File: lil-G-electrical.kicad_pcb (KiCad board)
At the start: 2 copper layers, 65 x 56 mm, 7 parts, among them J1 GPIO, U2 TPS565208

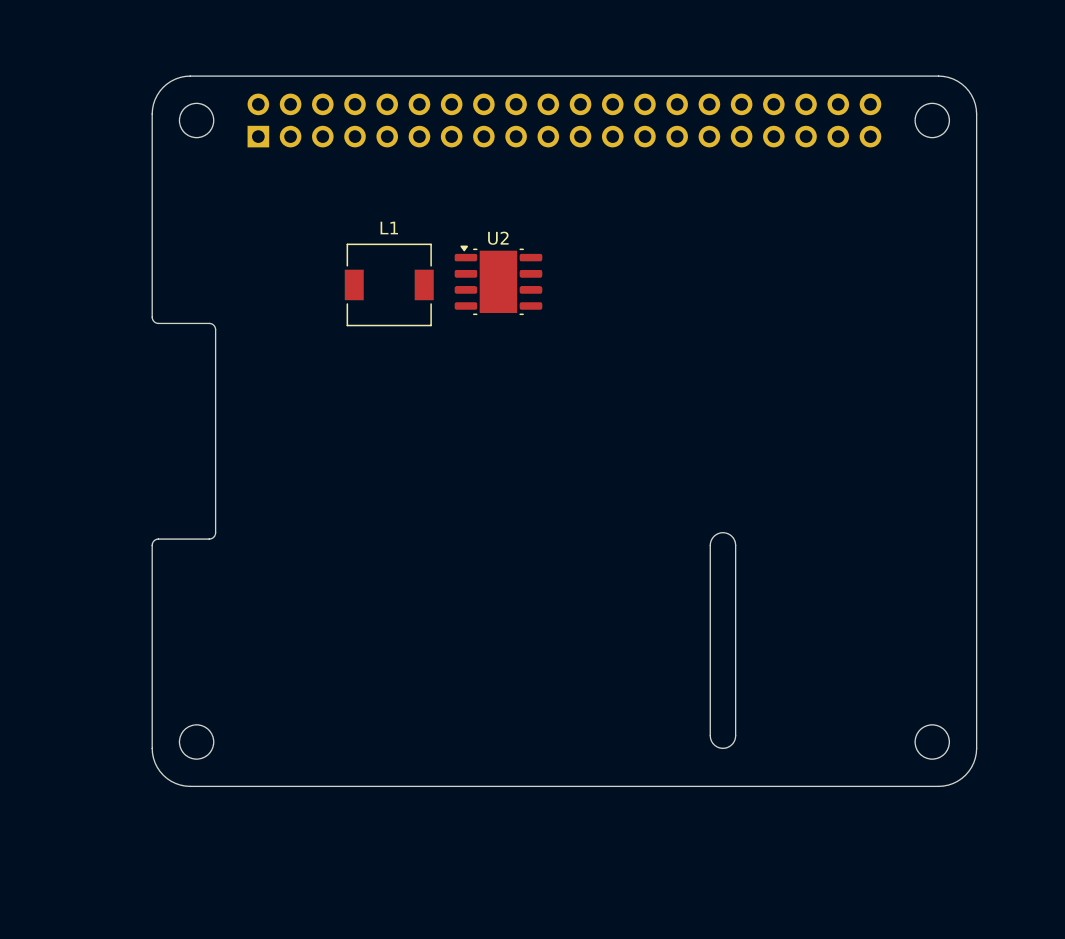
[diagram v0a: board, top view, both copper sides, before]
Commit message: finished layout of dc drivers and power regulation
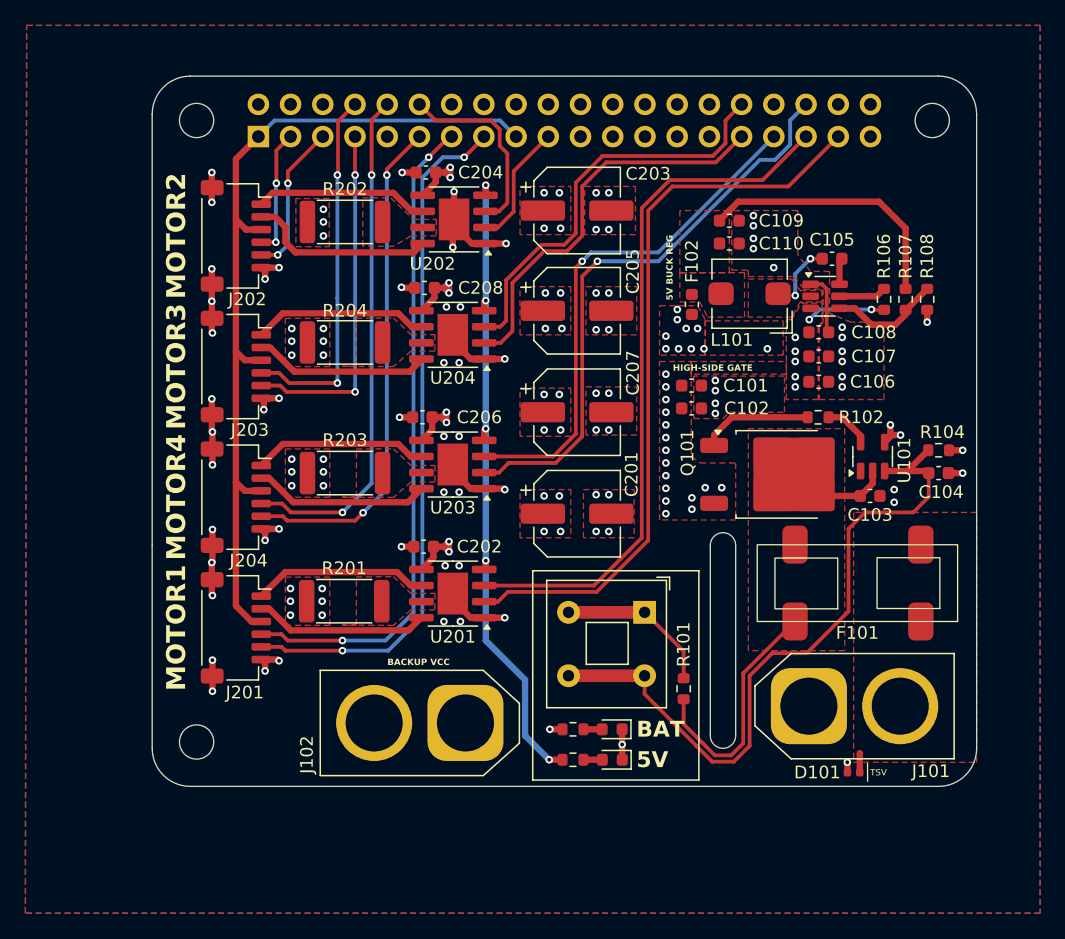
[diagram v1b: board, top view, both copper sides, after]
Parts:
- removed MH4: MountingHole_2.7mm_M2.5, MountingHole:MountingHole_2.7mm_M2.5
- added C101: 22uF, Capacitor_SMD:C_0603_1608Metric, F.Cu at (142.5, 68.4)
- added C102: 22uF, Capacitor_SMD:C_0603_1608Metric, F.Cu at (142.5, 70.2)
- added C103: 10uF, Capacitor_SMD:C_0603_1608Metric, F.Cu at (156.6, 77.1)
- added C104: 0.1uF, Capacitor_SMD:C_0603_1608Metric, F.Cu at (162.0, 75.3)
- added C105: 0.1uF, Capacitor_SMD:C_0603_1608Metric, F.Cu at (153.6, 58.4)
- added C106: 10uF, Capacitor_SMD:C_0603_1608Metric, F.Cu at (152.6, 68.1)
- added C107: 10uF, Capacitor_SMD:C_0603_1608Metric, F.Cu at (152.6, 66.1)
- added C108: 0.1uF, Capacitor_SMD:C_0603_1608Metric, F.Cu at (152.6, 64.2)
- added C109: 22uF, Capacitor_SMD:C_0603_1608Metric, F.Cu at (145.5, 55.4)
- added C110: 22uF, Capacitor_SMD:C_0603_1608Metric, F.Cu at (145.5, 57.2)
- added C201: 100uF, Capacitor_SMD:CP_Elec_6.3x7.7, F.Cu at (133.5, 78.5)
- added C202: 0.22uF, Capacitor_SMD:C_0603_1608Metric, F.Cu at (121.4, 81.1)
- added C203: 100uF, Capacitor_SMD:CP_Elec_6.3x7.7, F.Cu at (133.5, 54.6)
- added C204: 0.22uF, Capacitor_SMD:C_0603_1608Metric, F.Cu at (121.6, 51.6)
- added C205: 100uF, Capacitor_SMD:CP_Elec_6.3x7.7, F.Cu at (133.5, 62.5)
- added C206: 0.22uF, Capacitor_SMD:C_0603_1608Metric, F.Cu at (121.3, 70.9)
- added C207: 100uF, Capacitor_SMD:CP_Elec_6.3x7.7, F.Cu at (133.5, 70.5)
- added C208: 0.22uF, Capacitor_SMD:C_0603_1608Metric, F.Cu at (121.5, 60.7)
- added D101: GG0402126R042P, Diode_SMD:D_0402_1005Metric, F.Cu at (155.3, 98.9)
- added D102: GREEN, LED_SMD:LED_0603_1608Metric, F.Cu at (136.3, 95.5)
- added D103: GREEN, LED_SMD:LED_0603_1608Metric, F.Cu at (136.3, 97.9)
- added F101: 10A, lilG_footprints:LittleFuse_Mini_100_SMD, F.Cu at (155.6, 84.0)
- added F102: 5A, Fuse:Fuse_0603_1608Metric, F.Cu at (142.6, 62.0)
- added J101: XT-60, Connector_AMASS:AMASS_XT60-M_1x02_P7.20mm_Vertical, F.Cu at (151.8, 93.7)
- added J102: XT-60, Connector_AMASS:AMASS_XT60-M_1x02_P7.20mm_Vertical, F.Cu at (124.7, 95.0)
- added J201: JST-SH, Connector_JST:JST_SH_SM06B-SRSS-TB_1x06-1MP_P1.00mm_Horizontal, F.Cu at (106.6, 87.5)
- added J202: JST-SH, Connector_JST:JST_SH_SM06B-SRSS-TB_1x06-1MP_P1.00mm_Horizontal, F.Cu at (106.6, 56.6)
- added J203: JST-SH, Connector_JST:JST_SH_SM06B-SRSS-TB_1x06-1MP_P1.00mm_Horizontal, F.Cu at (106.6, 66.9)
- added J204: JST-SH, Connector_JST:JST_SH_SM06B-SRSS-TB_1x06-1MP_P1.00mm_Horizontal, F.Cu at (106.6, 77.2)
- added Q101: STD26P3LLH6, Package_TO_SOT_SMD:TO-252-2, F.Cu at (149.3, 75.4)
- added R101: 10k, Resistor_SMD:R_0603_1608Metric, F.Cu at (141.9, 92.3)
- added R102: 22, Resistor_SMD:R_0603_1608Metric, F.Cu at (152.5, 70.9)
- added R103: 10k, Resistor_SMD:R_0603_1608Metric, F.Cu at (133.2, 95.5)
- added R104: 10k, Resistor_SMD:R_0603_1608Metric, F.Cu at (162.0, 73.5)
- added R105: 1k, Resistor_SMD:R_0603_1608Metric, F.Cu at (133.2, 97.9)
- added R106: 10k, Resistor_SMD:R_0603_1608Metric, F.Cu at (157.7, 61.6)
- added R107: 54.9k, Resistor_SMD:R_0603_1608Metric, F.Cu at (159.4, 61.6)
- added R108: 10k, Resistor_SMD:R_0603_1608Metric, F.Cu at (161.1, 61.6)
- added R201: 500m, Resistor_SMD:R_2512_6332Metric, F.Cu at (115.1, 85.4)
- added R202: 500m, Resistor_SMD:R_2512_6332Metric, F.Cu at (115.2, 55.5)
- added R203: 500m, Resistor_SMD:R_2512_6332Metric, F.Cu at (115.2, 75.3)
- added R204: 500m, Resistor_SMD:R_2512_6332Metric, F.Cu at (115.2, 65.0)
- added SW101: PVA1EE, Button_Switch_THT:SW_Push_2P1T_Toggle_CK_PVA1xxH4xxxxxxV2, F.Cu at (138.8, 86.3)
- added U101: MCP1415, Package_TO_SOT_SMD:SOT-23-5, F.Cu at (156.8, 74.0)
- added U201: A4950E, Package_SO:SOIC-8-1EP_3.9x4.9mm_P1.27mm_EP2.41x3.3mm, F.Cu at (123.7, 84.8)
- added U202: A4950E, Package_SO:SOIC-8-1EP_3.9x4.9mm_P1.27mm_EP2.41x3.3mm, F.Cu at (123.8, 55.3)
- added U203: A4950E, Package_SO:SOIC-8-1EP_3.9x4.9mm_P1.27mm_EP2.41x3.3mm, F.Cu at (123.7, 74.6)
- added U204: A4950E, Package_SO:SOIC-8-1EP_3.9x4.9mm_P1.27mm_EP2.41x3.3mm, F.Cu at (123.7, 64.4)
- L101: renamed from L1; value L_Small -> 3.3uH; footprint Inductor_SMD:L_6.3x6.3_H3 -> Inductor_SMD:L_Bourns_SRP5030T
- U102: renamed from U2; footprint Package_SO:Texas_R-PDSO-G8_EP2.95x4.9mm_Mask2.4x3.1mm -> Package_TO_SOT_SMD:SOT-23-6
- moved L101 28.4 mm to (147.1, 61.2), turned to 180 degrees
- moved U102 25.8 mm to (153.1, 61.4)
- renumbered J1 to J103
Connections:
- J103 pad 10: /GPIO15/RXD0 -> /M4_ENC_A
- J103 pad 11: /GPIO17 -> /M4_ENC_B
- J103 pad 12: /GPIO18/PCM.CLK -> /M2_PWM
- J103 pad 13: /GPIO27 -> /M1_ENC_A
- J103 pad 15: /GPIO22 -> /M1_ENC_B
- J103 pad 16: /GPIO23 -> unconnected-(J103-Pin_16-Pad16)
- J103 pad 18: /GPIO24 -> unconnected-(J103-Pin_18-Pad18)
- J103 pad 19: /GPIO10/SPI0.MOSI -> /M2_DIR
- J103 pad 21: /GPIO9/SPI0.MISO -> unconnected-(J103-Pin_21-Pad21)
- J103 pad 22: /GPIO25 -> unconnected-(J103-Pin_22-Pad22)
- J103 pad 23: /GPIO11/SPI0.SCLK -> unconnected-(J103-Pin_23-Pad23)
- J103 pad 24: /GPIO8/SPI0.CE0 -> unconnected-(J103-Pin_24-Pad24)
- J103 pad 26: /GPIO7/SPI0.CE1 -> unconnected-(J103-Pin_26-Pad26)
- J103 pad 27: /ID_SDA -> unconnected-(J103-Pin_27-Pad27)
- J103 pad 28: /ID_SCL -> unconnected-(J103-Pin_28-Pad28)
- J103 pad 29: /GPIO5 -> unconnected-(J103-Pin_29-Pad29)
- J103 pad 3: /GPIO2/SDA1 -> /M2_ENC_A
- J103 pad 31: /GPIO6 -> /M3_DIR
- J103 pad 32: /GPIO12/PWM0 -> /M3_PWM
- J103 pad 33: /GPIO13/PWM1 -> /M4_PWM
- J103 pad 35: /GPIO19/PCM.FS -> /M1_PWM
- J103 pad 36: /GPIO16 -> /M4_DIR
- J103 pad 37: /GPIO26 -> /M1_DIR
- J103 pad 38: /GPIO20/PCM.DIN -> unconnected-(J103-Pin_38-Pad38)
- J103 pad 40: /GPIO21/PCM.DOUT -> unconnected-(J103-Pin_40-Pad40)
- J103 pad 5: /GPIO3/SCL1 -> /M2_ENC_B
- J103 pad 7: /GPIO4/GPCLK0 -> /M3_ENC_B
- J103 pad 8: /GPIO14/TXD0 -> /M3_ENC_A
- L101 pad 1: unconnected-(L1-Pad1) -> Net-(U102-SW)
- L101 pad 2: unconnected-(L1-Pad2) -> Net-(C109-Pad1)
- U102 pad 1: unconnected-(U2-GND-Pad1) -> GND
- U102 pad 2: unconnected-(U2-SW-Pad2) -> Net-(U102-SW)
- U102 pad 3: unconnected-(U2-VIN-Pad3) -> VCC
- U102 pad 4: unconnected-(U2-VFB-Pad4) -> Net-(U102-VFB)
- U102 pad 5: unconnected-(U2-EN-Pad5) -> Net-(U102-EN)
- U102 pad 6: unconnected-(U2-VBST-Pad6) -> Net-(U102-VBST)
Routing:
- net +5V: track 0.00 -> 79.1 mm, vias 0 -> 15
- net +3V3: track 0.00 -> 68.5 mm
- net GND: track 0.00 -> 67.8 mm, vias 0 -> 104
- net /M1_DIR: track 0.00 -> 58.3 mm
- net /PWR_EN: track 0.00 -> 55.5 mm
- net /M1_PWM: track 0.00 -> 55.3 mm
- net /M1_ENC_B: track 0.00 -> 54.8 mm, vias 0 -> 2
- net /M1_ENC_A: track 0.00 -> 52.0 mm, vias 0 -> 2
- net /M4_DIR: track 0.00 -> 45.9 mm, vias 0 -> 1
- net /M4_PWM: track 0.00 -> 41.0 mm, vias 0 -> 1
- net /M4_ENC_A: track 0.00 -> 40.3 mm, vias 0 -> 2
- net /M4_ENC_B: track 0.00 -> 39.9 mm, vias 0 -> 2
- net /M3_PWM: track 0.00 -> 32.8 mm
- net /M3_DIR: track 0.00 -> 31.5 mm
- net /M3_ENC_A: track 0.00 -> 28.9 mm, vias 0 -> 2
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- added copper zone on F.Cu, net +5V
- added copper zone on In2.Cu, net +5V
- added copper zone on B.Cu, net GND
- added copper zone on F.Cu, net GND
- added copper zone on In1.Cu, net GND
- added copper zone on F.Cu, net Net-(C109-Pad1)
- added copper zone on F.Cu, net Net-(D101-K)
- added copper zone on F.Cu, net Net-(Q101-D)
- added copper zone on F.Cu, net Net-(U102-SW)
- added copper zone on F.Cu, net Net-(U201-LSS)
- added copper zone on F.Cu, net Net-(U202-LSS)
- added copper zone on F.Cu, net Net-(U203-LSS)
- added copper zone on F.Cu, net Net-(U204-LSS)
- added copper zone on F.Cu, net VCC
- added copper zone on In2.Cu, net VCC
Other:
- outline, holes or cut-outs redrawn
- copper layers 2 -> 4
- board text added: "5V"
- board text added: "5V BUCK REG"
- board text added: "BACKUP VCC"
- board text added: "BAT"
- board text added: "HIGH-SIDE GATE"
- board text added: "MOTOR1"
- board text added: "MOTOR2"
- board text added: "MOTOR3"
- board text added: "MOTOR4"
- board text added: "TSV"

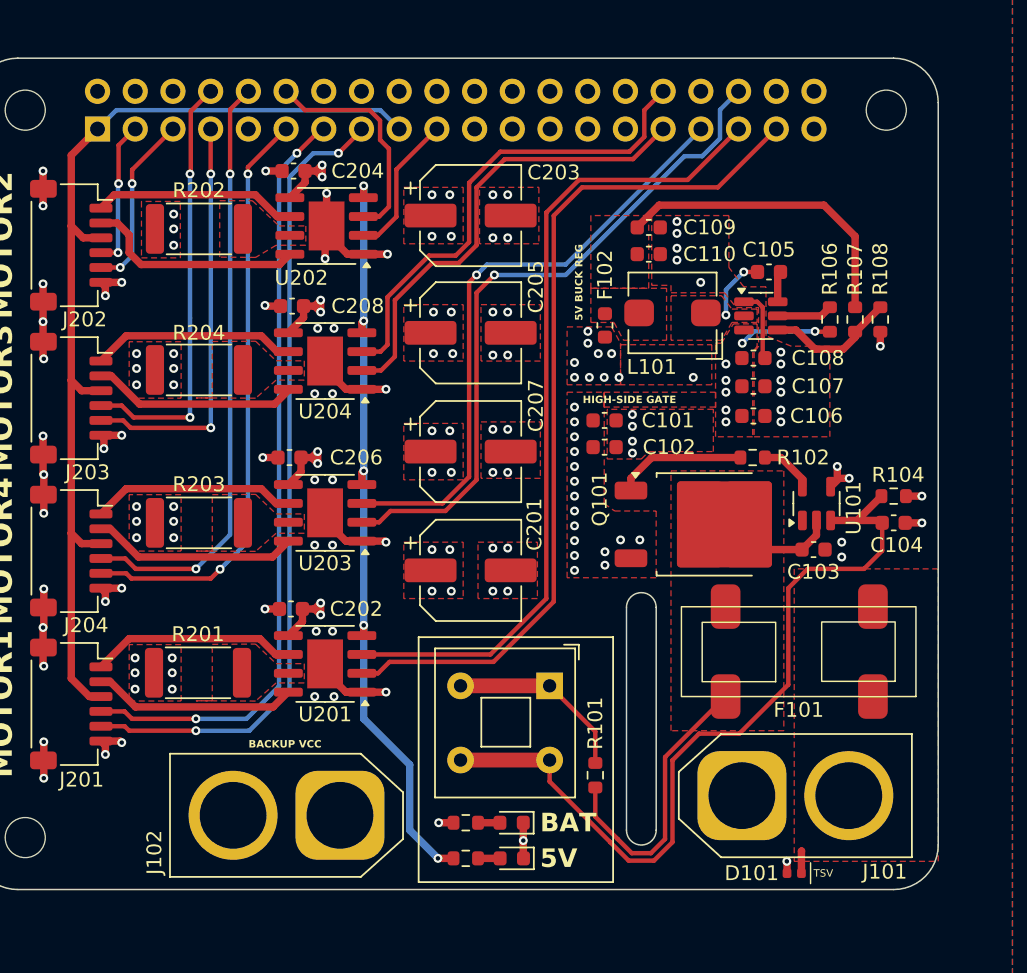
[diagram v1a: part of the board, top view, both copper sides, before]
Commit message: changed dimension of current sense resistor
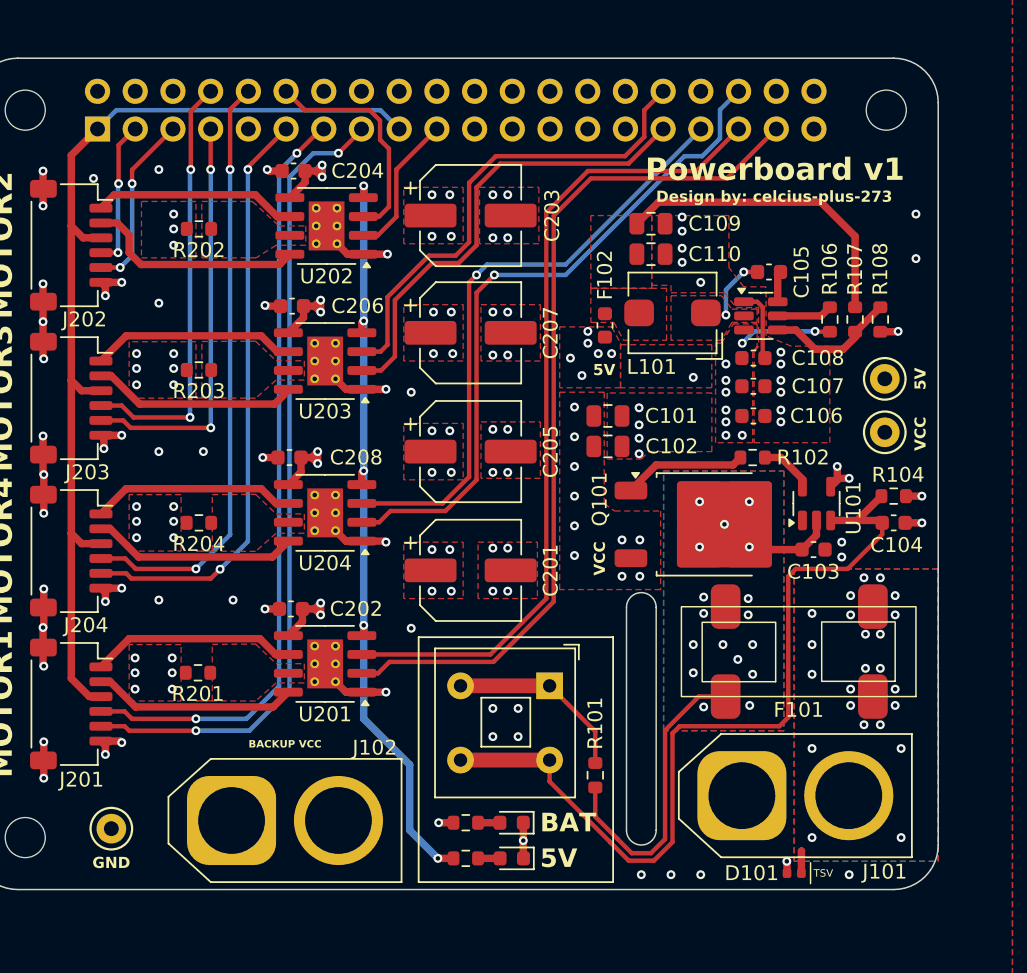
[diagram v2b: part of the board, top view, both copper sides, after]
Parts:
- added TP101: TestPoint, TestPoint:TestPoint_Keystone_5000-5004_Miniature, F.Cu at (161.4, 69.2)
- added TP102: TestPoint, TestPoint:TestPoint_Keystone_5000-5004_Miniature, F.Cu at (109.3, 95.9)
- added TP103: TestPoint, TestPoint:TestPoint_Keystone_5000-5004_Miniature, F.Cu at (161.4, 65.6)
- C101, C102, C109, C110: footprint Capacitor_SMD:C_0603_1608Metric -> Capacitor_SMD:C_0805_2012Metric
- F101: value 10A -> 01000065Z
- F102: value 5A -> 0686F5000
- R201, R202: footprint Resistor_SMD:R_2512_6332Metric -> Resistor_SMD:R_0603_1608Metric
- R203: renamed from R204; footprint Resistor_SMD:R_2512_6332Metric -> Resistor_SMD:R_0603_1608Metric
- R204: renamed from R203; footprint Resistor_SMD:R_2512_6332Metric -> Resistor_SMD:R_0603_1608Metric
- U201, U202: footprint Package_SO:SOIC-8-1EP_3.9x4.9mm_P1.27mm_EP2.41x3.3mm -> Package_SO:SOIC-8-1EP_3.9x4.9mm_P1.27mm_EP2.41x3.3mm_ThermalVias
- U203: renamed from U204; footprint Package_SO:SOIC-8-1EP_3.9x4.9mm_P1.27mm_EP2.41x3.3mm -> Package_SO:SOIC-8-1EP_3.9x4.9mm_P1.27mm_EP2.41x3.3mm_ThermalVias
- U204: renamed from U203; footprint Package_SO:SOIC-8-1EP_3.9x4.9mm_P1.27mm_EP2.41x3.3mm -> Package_SO:SOIC-8-1EP_3.9x4.9mm_P1.27mm_EP2.41x3.3mm_ThermalVias
- moved J102 7.31 mm to (117.4, 95.3), turned to 0 degrees
- moved C101 0.38 mm to (142.8, 68.1)
- moved C109 0.29 mm to (145.7, 55.1)
- moved C102 0.23 mm to (142.8, 70.2)
- moved C110 0.15 mm to (145.7, 57.2)
- renumbered C207 to C205, C208 to C206, C205 to C207, C206 to C208
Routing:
- net VCC: track 26.8 -> 59.9 mm, vias 48 -> 44
- net +5V: track 79.1 -> 109.9 mm, vias 15 -> 12
- net GND: track 67.8 -> 63.5 mm, vias 104 -> 109
- net /PWR_EN: track 55.5 -> 57.7 mm
- net Net-(Q101-D): track 25.4 -> 26.4 mm, vias 0 -> 17
- net Net-(D101-K): vias 0 -> 23
- added copper zone on B.Cu, net Net-(D101-K)
- added copper zone on B.Cu, net Net-(Q101-D)
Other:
- board text added: "Design by: celcius-plus-273"
- board text added: "GND"
- board text added: "Powerboard v1"
- board text added: "VCC"
- board text removed: "5V BUCK REG"
- board text removed: "HIGH-SIDE GATE"

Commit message: version 2 done
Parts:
- removed C101, C102, C109, C110: 22uF, Capacitor_SMD:C_0805_2012Metric
- removed C103, C106, C107: 10uF, Capacitor_SMD:C_0603_1608Metric
- removed C104, C105, C108: 0.1uF, Capacitor_SMD:C_0603_1608Metric
- removed C201, C203, C205, C207: 100uF, Capacitor_SMD:CP_Elec_6.3x7.7
- removed C202, C204, C206, C208: 0.22uF, Capacitor_SMD:C_0603_1608Metric
- removed D101: GG0402126R042P, Diode_SMD:D_0402_1005Metric
- removed D102, D103: GREEN, LED_SMD:LED_0603_1608Metric
- removed F101: 01000065Z, lilG_footprints:LittleFuse_Mini_100_SMD
- removed F102: 0686F5000, Fuse:Fuse_0603_1608Metric
- removed J101, J102: XT-60, Connector_AMASS:AMASS_XT60-M_1x02_P7.20mm_Vertical
- removed J103: GPIO, Connector_PinSocket_2.54mm:PinSocket_2x20_P2.54mm_Vertical
- removed J201, J202, J203, J204: JST-SH, Connector_JST:JST_SH_SM06B-SRSS-TB_1x06-1MP_P1.00mm_Horizontal
- removed L101: 3.3uH, Inductor_SMD:L_Bourns_SRP5030T
- removed Q101: STD26P3LLH6, Package_TO_SOT_SMD:TO-252-2
- removed R101, R103, R104, R106, R108: 10k, Resistor_SMD:R_0603_1608Metric
- removed R102: 22, Resistor_SMD:R_0603_1608Metric
- removed R105: 1k, Resistor_SMD:R_0603_1608Metric
- removed R107: 54.9k, Resistor_SMD:R_0603_1608Metric
- removed R201, R202, R203, R204: 500m, Resistor_SMD:R_0603_1608Metric
- removed SW101: PVA1EE, Button_Switch_THT:SW_Push_2P1T_Toggle_CK_PVA1xxH4xxxxxxV2
- removed TP101, TP102, TP103: TestPoint, TestPoint:TestPoint_Keystone_5000-5004_Miniature
- removed U101: MCP1415, Package_TO_SOT_SMD:SOT-23-5
- removed U102: TPS565208, Package_TO_SOT_SMD:SOT-23-6
- removed U201, U202, U203, U204: A4950E, Package_SO:SOIC-8-1EP_3.9x4.9mm_P1.27mm_EP2.41x3.3mm_ThermalVias
- added C1: 22uF, Capacitor_SMD:C_0805_2012Metric, F.Cu at (101.8, 97.2)
- added C10: 22uF, Capacitor_SMD:C_0805_2012Metric, F.Cu at (107.2, 90.3)
- added C11: 10uF, Capacitor_SMD:C_0603_1608Metric, F.Cu at (76.8, 95.5)
- added C12: 10uF, Capacitor_SMD:C_0603_1608Metric, F.Cu at (74.1, 96.2)
- added C13: 100n, Capacitor_SMD:C_0402_1005Metric, F.Cu at (77.2, 76.2)
- added C15: 100n, Capacitor_SMD:C_0402_1005Metric, F.Cu at (81.8, 81.0)
- added C16: 100n, Capacitor_SMD:C_0402_1005Metric, F.Cu at (85.6, 83.8)
- added C17: 100n, Capacitor_SMD:C_0402_1005Metric, F.Cu at (90.2, 71.9)
- added C18: 100n, Capacitor_SMD:C_0402_1005Metric, F.Cu at (91.5, 84.2)
- added C19: 100n, Capacitor_SMD:C_0402_1005Metric, F.Cu at (94.9, 73.9)
- added C2: 22uF, Capacitor_SMD:C_0805_2012Metric, F.Cu at (99.3, 97.2)
- added C20: 100n, Capacitor_SMD:C_0402_1005Metric, F.Cu at (86.0, 71.9)
- added C21: 100n, Capacitor_SMD:C_0402_1005Metric, F.Cu at (96.8, 80.3)
- added C22: 4.7u, Capacitor_SMD:C_0402_1005Metric, F.Cu at (96.8, 77.7)
- added C23: 100n, Capacitor_SMD:C_0402_1005Metric, F.Cu at (89.0, 84.7)
- added C24: 100n, Capacitor_SMD:C_0402_1005Metric, F.Cu at (89.1, 71.9)
- added C25: 100n, Capacitor_SMD:C_0402_1005Metric, F.Cu at (60.1, 82.7)
- added C26: 4.7u, Capacitor_SMD:C_0402_1005Metric, F.Cu at (84.1, 76.5)
- added C27: 4.7u, Capacitor_SMD:C_0402_1005Metric, F.Cu at (84.4, 74.0)
- added C28: 4.7u, Capacitor_SMD:C_0402_1005Metric, F.Cu at (85.1, 76.5)
- added C29: 15p, Capacitor_SMD:C_0402_1005Metric, F.Cu at (98.9, 80.7)
- added C3: 10uF, Capacitor_SMD:C_0603_1608Metric, F.Cu at (87.6, 100.4)
- added C30: 15p, Capacitor_SMD:C_0402_1005Metric, F.Cu at (98.9, 78.3)
- added C31: 10uF, Capacitor_SMD:C_0603_1608Metric, F.Cu at (61.5, 83.3)
- added C32: 10uF, Capacitor_SMD:C_0603_1608Metric, F.Cu at (62.2, 96.2)
- added C33: 100n, Capacitor_SMD:C_0402_1005Metric, F.Cu at (88.9, 91.2)
- added C34: 100n, Capacitor_SMD:C_0402_1005Metric, F.Cu at (92.4, 90.5)
- added C35: 100uF, Capacitor_SMD:CP_Elec_6.3x7.7, F.Cu at (60.0, 62.8)
- added C36: 0.22uF, Capacitor_SMD:C_0603_1608Metric, F.Cu at (71.0, 61.2)
- added C37: 100uF, Capacitor_SMD:CP_Elec_6.3x7.7, F.Cu at (76.8, 63.0)
- added C38: 0.22uF, Capacitor_SMD:C_0603_1608Metric, F.Cu at (87.6, 61.1)
- added C39: 100uF, Capacitor_SMD:CP_Elec_6.3x7.7, F.Cu at (93.2, 63.0)
- added C4: 100n, Capacitor_SMD:C_0402_1005Metric, F.Cu at (85.5, 97.8)
- added C40: 0.22uF, Capacitor_SMD:C_0603_1608Metric, F.Cu at (104.1, 61.1)
- added C41: 100uF, Capacitor_SMD:CP_Elec_6.3x7.7, F.Cu at (109.9, 63.1)
- added C42: 0.22uF, Capacitor_SMD:C_0603_1608Metric, F.Cu at (120.9, 61.1)
- added C43: 100n, Capacitor_SMD:C_0402_1005Metric, F.Cu at (77.0, 83.9)
- added C5: 100n, Capacitor_SMD:C_0402_1005Metric, F.Cu at (114.9, 98.7)
- added C6: 10uF, Capacitor_SMD:C_0603_1608Metric, F.Cu at (107.8, 96.9)
- added C7: 10uF, Capacitor_SMD:C_0603_1608Metric, F.Cu at (105.9, 96.9)
- added C8: 100n, Capacitor_SMD:C_0402_1005Metric, F.Cu at (109.5, 97.1)
- added C9: 22uF, Capacitor_SMD:C_0805_2012Metric, F.Cu at (109.5, 90.3)
- added D1: KT-0805G, LED_SMD:LED_0805_2012Metric, F.Cu at (55.2, 105.9)
- added D10: KT-0603R, LED_SMD:LED_0603_1608Metric, F.Cu at (55.5, 92.0)
- added D11: KT-0805G, LED_SMD:LED_0805_2012Metric, F.Cu at (64.5, 76.4)
- added D2: GG0402126R042P, Diode_SMD:D_0402_1005Metric, F.Cu at (82.9, 106.4)
- added D3: KT-0805G, LED_SMD:LED_0805_2012Metric, F.Cu at (55.2, 108.4)
- added D4: KT-0603W, LED_SMD:LED_0603_1608Metric, F.Cu at (106.7, 80.3)
- added D5: KT-0603W, LED_SMD:LED_0603_1608Metric, F.Cu at (108.7, 80.3)
- added D6: KT-0603W, LED_SMD:LED_0603_1608Metric, F.Cu at (110.7, 80.3)
- added D7: KT-0603W, LED_SMD:LED_0603_1608Metric, F.Cu at (112.7, 80.3)
- added D8: KT-0805G, LED_SMD:LED_0805_2012Metric, F.Cu at (55.2, 110.9)
- added D9: KT-0603R, LED_SMD:LED_0603_1608Metric, F.Cu at (55.5, 86.1)
- added F1: 01530007Z, lilG_footprints:LittleFuse_01530007Z, F.Cu at (89.8, 116.6)
- added F2: S0603-S-5.0A, Fuse:Fuse_0603_1608Metric, F.Cu at (119.3, 93.8)
- added F3: 0467001.NRHF, Fuse:Fuse_0603_1608Metric, F.Cu at (70.1, 96.2)
- added F4: 0467001.NRHF, Fuse:Fuse_0603_1608Metric, F.Cu at (66.2, 96.2)
- added J1: XT60-PW-M, Connector_AMASS:AMASS_XT60PW-M_1x02_P7.20mm_Horizontal, F.Cu at (76.0, 104.0)
- added J10: BM06B-SRSS-TB, Connector_JST:JST_SH_BM06B-SRSS-TB_1x06-1MP_P1.00mm_Vertical, F.Cu at (81.5, 52.4)
- added J11: BM06B-SRSS-TB, Connector_JST:JST_SH_BM06B-SRSS-TB_1x06-1MP_P1.00mm_Vertical, F.Cu at (98.1, 52.4)
- added J12: BM06B-SRSS-TB, Connector_JST:JST_SH_BM06B-SRSS-TB_1x06-1MP_P1.00mm_Vertical, F.Cu at (114.8, 52.4)
- added J2: XT30-U-M, Connector_AMASS:AMASS_XT30U-M_1x02_P5.0mm_Vertical, F.Cu at (126.1, 103.0)
- added J3: XT60-PW-M, Connector_AMASS:AMASS_XT60PW-M_1x02_P7.20mm_Horizontal, F.Cu at (110.7, 104.0)
- added J4: BM04B-SRSS-TB, Connector_JST:JST_SH_BM04B-SRSS-TB_1x04-1MP_P1.00mm_Vertical, F.Cu at (126.4, 88.5)
- added J5: BM03B-SRSS-TB, Connector_JST:JST_SH_BM03B-SRSS-TB_1x03-1MP_P1.00mm_Vertical, F.Cu at (126.4, 81.0)
- added J6: BM03B-SRSS-TB, Connector_JST:JST_SH_BM03B-SRSS-TB_1x03-1MP_P1.00mm_Vertical, F.Cu at (126.4, 73.6)
- added J7: TC2030-NL, Connector:Tag-Connect_TC2030-IDC-NL_2x03_P1.27mm_Vertical, F.Cu at (127.0, 66.3)
- added J8: TYPE-C16PIN, Connector_USB:USB_C_Receptacle_GCT_USB4105-xx-A_16P_TopMnt_Horizontal, F.Cu at (53.4, 76.4)
- added J9: BM06B-SRSS-TB, Connector_JST:JST_SH_BM06B-SRSS-TB_1x06-1MP_P1.00mm_Vertical, F.Cu at (64.8, 52.4)
- added L1: SRP5030T-3R3M, Inductor_SMD:L_Bourns_SRP5030T, F.Cu at (114.5, 92.3)
- added L2: AOTA-B201610S3R3-101-T, lilG_footprints:L_0806, F.Cu at (82.5, 76.5)
- added MH4: MountingHole_2.7mm_M2.5, MountingHole:MountingHole_2.7mm_M2.5, F.Cu at (132.8, 129.4)
- added Q1: 40P30, Package_TO_SOT_SMD:TO-252-2, F.Cu at (94.0, 99.7)
- added R1: 10k, Resistor_SMD:R_0402_1005Metric, F.Cu at (62.7, 114.7)
- added R10: 1k, Resistor_SMD:R_0402_1005Metric, F.Cu at (112.0, 77.2)
- added R11: 1k, Resistor_SMD:R_0402_1005Metric, F.Cu at (113.1, 77.2)
- added R12: 1k, Resistor_SMD:R_0402_1005Metric, F.Cu at (114.2, 77.2)
- added R13: 1k, Resistor_SMD:R_0402_1005Metric, F.Cu at (60.3, 101.0)
- added R14: 300k, Resistor_SMD:R_0603_1608Metric, F.Cu at (76.7, 73.0)
- added R15: 100k, Resistor_SMD:R_0603_1608Metric, F.Cu at (76.7, 74.7)
- added R16: 1k, Resistor_SMD:R_0402_1005Metric, F.Cu at (51.4, 82.6)
- added R2: 4.7k, Resistor_SMD:R_0402_1005Metric, F.Cu at (57.7, 101.0)
- added R20: 27, Resistor_SMD:R_0402_1005Metric, F.Cu at (81.8, 79.9)
- added R21: 27, Resistor_SMD:R_0402_1005Metric, F.Cu at (81.8, 78.8)
- added R22: 33, Resistor_SMD:R_0402_1005Metric, F.Cu at (84.4, 72.8)
- added R24: 1k, Resistor_SMD:R_0402_1005Metric, F.Cu at (96.8, 78.9)
- added R25: 1k, Resistor_SMD:R_0402_1005Metric, F.Cu at (51.6, 95.5)
- added R26: 5.1k, Resistor_SMD:R_0402_1005Metric, F.Cu at (55.8, 70.4)
- added R27: 5.1k, Resistor_SMD:R_0402_1005Metric, F.Cu at (55.8, 69.2)
- added R28: 1k, Resistor_SMD:R_0402_1005Metric, F.Cu at (64.5, 74.0)
- added R29: 4.7k, Resistor_SMD:R_0402_1005Metric, F.Cu at (115.3, 83.4)
- added R3: 22, Resistor_SMD:R_0402_1005Metric, F.Cu at (85.5, 103.1)
- added R30: 4.7k, Resistor_SMD:R_0402_1005Metric, F.Cu at (115.3, 79.4)
- added R31: 200k, Resistor_SMD:R_0402_1005Metric, F.Cu at (71.3, 66.1)
- added R32: 50k, Resistor_SMD:R_0402_1005Metric, F.Cu at (71.3, 64.8)
- added R33: RL10FTNR100, Resistor_SMD:R_0805_2012Metric, F.Cu at (66.4, 57.1)
- added R34: 200k, Resistor_SMD:R_0402_1005Metric, F.Cu at (87.8, 66.1)
- added R35: 50k, Resistor_SMD:R_0402_1005Metric, F.Cu at (87.8, 64.8)
- added R36: RL10FTNR100, Resistor_SMD:R_0805_2012Metric, F.Cu at (83.1, 57.1)
- added R37: 200k, Resistor_SMD:R_0402_1005Metric, F.Cu at (104.3, 66.1)
- added R38: 50k, Resistor_SMD:R_0402_1005Metric, F.Cu at (104.3, 64.8)
- added R39: RL10FTNR100, Resistor_SMD:R_0805_2012Metric, F.Cu at (99.5, 57.1)
- added R4: 10k, Resistor_SMD:R_0402_1005Metric, F.Cu at (85.5, 96.6)
- added R40: 200k, Resistor_SMD:R_0402_1005Metric, F.Cu at (121.0, 66.1)
- added R41: 50k, Resistor_SMD:R_0402_1005Metric, F.Cu at (121.0, 64.9)
- added R42: RL10FTNR100, Resistor_SMD:R_0805_2012Metric, F.Cu at (116.2, 57.1)
- added R5: 1k, Resistor_SMD:R_0402_1005Metric, F.Cu at (59.0, 101.0)
- added R6: 10k, Resistor_SMD:R_0402_1005Metric, F.Cu at (117.3, 101.8)
- added R7: 54.9k, Resistor_SMD:R_0402_1005Metric, F.Cu at (117.3, 103.0)
- added R8: 10k, Resistor_SMD:R_0402_1005Metric, F.Cu at (117.3, 104.3)
- added R9: 1k, Resistor_SMD:R_0402_1005Metric, F.Cu at (110.9, 77.2)
- added SW1: 5.8 ZSGT, lilG_footprints:5.8_ZSGT, F.Cu at (57.0, 116.8)
- added SW2: KMR2, Button_Switch_SMD:SW_Push_1P1T_NO_CK_KMR2, F.Cu at (52.2, 86.1)
- added SW3: KMR2, Button_Switch_SMD:SW_Push_1P1T_NO_CK_KMR2, F.Cu at (52.2, 92.0)
- added TP1: 5001, TestPoint:TestPoint_Keystone_5000-5004_Miniature, F.Cu at (118.8, 112.4)
- added TP2: 5001, TestPoint:TestPoint_Keystone_5000-5004_Miniature, F.Cu at (122.8, 118.4)
- added TP3: 5001, TestPoint:TestPoint_Keystone_5000-5004_Miniature, F.Cu at (122.8, 112.4)
- added TP4: 5001, TestPoint:TestPoint_Keystone_5000-5004_Miniature, F.Cu at (118.8, 79.4)
- added TP5: 5001, TestPoint:TestPoint_Keystone_5000-5004_Miniature, F.Cu at (118.8, 83.4)
- added TP6: 5001, TestPoint:TestPoint_Keystone_5000-5004_Miniature, F.Cu at (126.8, 112.4)
- added U1: MCP1415, Package_TO_SOT_SMD:SOT-23-5, F.Cu at (84.4, 100.2)
- added U10: A4950E, Package_SO:SOIC-8-1EP_3.9x4.9mm_P1.27mm_EP2.41x3.3mm_ThermalVias, F.Cu at (100.1, 62.9)
- added U11: A4950E, Package_SO:SOIC-8-1EP_3.9x4.9mm_P1.27mm_EP2.41x3.3mm_ThermalVias, F.Cu at (116.8, 62.9)
- added U12: W25Q128JVS, Package_SO:SOIC-8_5.23x5.23mm_P1.27mm, F.Cu at (80.5, 87.2)
- added U2: TPS565208, Package_TO_SOT_SMD:SOT-23-6, F.Cu at (112.3, 97.5)
- added U3: NCP1117ST33T3G, digikey-footprints:SOT-223, F.Cu at (72.1, 90.6)
- added U4: USBLC6-2SC6, Package_TO_SOT_SMD:SOT-23-6, F.Cu at (63.4, 80.0)
- added U5: RP2350A, lilG_footprints:QFN-60-1EP_7x7mm_P0.4mm_EP3.4x3.4mm_ThermalVias, F.Cu at (89.8, 78.5)
- added U6: NCP1117ST33T3G, digikey-footprints:SOT-223, F.Cu at (64.2, 90.6)
- added U7: LSM6DSM, Package_LGA:LGA-14_3x2.5mm_P0.5mm_LayoutBorder3x4y, F.Cu at (89.8, 88.9)
- added U8: A4950E, Package_SO:SOIC-8-1EP_3.9x4.9mm_P1.27mm_EP2.41x3.3mm_ThermalVias, F.Cu at (67.0, 62.9)
- added U9: A4950E, Package_SO:SOIC-8-1EP_3.9x4.9mm_P1.27mm_EP2.41x3.3mm_ThermalVias, F.Cu at (83.7, 62.9)
- added Y1: ABM8-272-T3, Crystal:Crystal_SMD_Abracon_ABM8G-4Pin_3.2x2.5mm, F.Cu at (101.5, 79.5)
- moved MH2 140.9 mm to (46.8, 129.4)
- moved MH3 60.6 mm to (132.8, 43.4)
- moved MH1 56.8 mm to (46.8, 43.4)
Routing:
- net +3V3: track 68.5 -> 329.4 mm, vias 0 -> 19
- net /rp2350a/~{RESET}: track 0.00 -> 91.2 mm, vias 0 -> 4
- net /M1_DIR: track 58.3 -> 0.00 mm
- net /rp2350a/SWCLK: track 0.00 -> 55.8 mm, vias 0 -> 3
- net /M1_PWM: track 55.3 -> 0.00 mm
- net /I2C_SCL: track 0.00 -> 55.0 mm, vias 0 -> 1
- net /I2C_SDA: track 0.00 -> 52.7 mm, vias 0 -> 1
- net +5V: track 109.9 -> 161.5 mm
- net /rp2350a/BOOTSEL: track 0.00 -> 49.3 mm, vias 0 -> 2
- net /rp2350a/SWDIO: track 0.00 -> 49.2 mm, vias 0 -> 2
- net /VBAT_FUSED: track 0.00 -> 46.2 mm, vias 0 -> 1
- net /M4_DIR: track 45.9 -> 0.00 mm, vias 1 -> 0
- net /SPI_RX: track 0.00 -> 43.8 mm
- net /SPI_CSn: track 0.00 -> 42.9 mm
- net /SPI_SCK: track 0.00 -> 42.2 mm
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- added copper zone on F.Cu, net +1V1
- added copper zone on In2.Cu, net +1V1
- added copper zone on F.Cu, net +3V3
- added copper zone on In2.Cu, net +3V3
- added copper zone on F.Cu, net /5V_RAW
- added copper zone on B.Cu, net /BAT_1
- added copper zone on F.Cu, net /BAT_1
- added copper zone on B.Cu, net /VBAT_FUSED
- added copper zone on F.Cu, net /VBAT_FUSED
- added copper zone on F.Cu, net /rp2350a/VREG_LX
- added copper zone on F.Cu, net Net-(C12-Pad1)
- added copper zone on F.Cu, net Net-(C32-Pad1)
- added copper zone on F.Cu, net Net-(U10-LSS)
- added copper zone on F.Cu, net Net-(U11-LSS)
- added copper zone on F.Cu, net Net-(U2-SW)
- added copper zone on F.Cu, net Net-(U8-LSS)
- added copper zone on F.Cu, net Net-(U9-LSS)
- removed copper zone on F.Cu, net Net-(C109-Pad1)
- removed copper zone on B.Cu, net Net-(D101-K)
- removed copper zone on F.Cu, net Net-(D101-K)
- removed copper zone on B.Cu, net Net-(Q101-D)
- removed copper zone on F.Cu, net Net-(Q101-D)
- removed copper zone on F.Cu, net Net-(U102-SW)
- removed copper zone on F.Cu, net Net-(U201-LSS)
- removed copper zone on F.Cu, net Net-(U202-LSS)
- removed copper zone on F.Cu, net Net-(U203-LSS)
- removed copper zone on F.Cu, net Net-(U204-LSS)
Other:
- board size 65 x 56 mm -> 100 x 100 mm
- board text added: "1"
- board text added: "2"
- board text added: "3"
- board text added: "3V3"
- board text added: "4"
- board text added: "BAT 1"
- board text added: "BAT 2"
- board text added: "BOOT"
- board text added: "DEBUG"
- board text added: "DOWN"
- board text added: "I2C"
- board text added: "POWER"
- board text added: "Powerboard v2.0"
- board text added: "RUN"
- board text added: "SCL"
- board text added: "SDA"
- board text added: "SPI"
- board text added: "SWD"
- board text added: "TC"
- board text added: "UP"
- board text added: "X"
- board text added: "Y"
- board text added: "Z"
- board text removed: "BACKUP VCC"
- board text removed: "BAT"
- board text removed: "CAMERA (OPTIONAL)"
- board text removed: "DISPLAY (OPTIONAL)"
- board text removed: "Extend PCB edge 0.5mm if using SMT header"
- board text removed: "PoE"
- board text removed: "Powerboard v1"
- board text removed: "RJ45"
